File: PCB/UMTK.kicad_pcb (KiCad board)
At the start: 4 copper layers, 170 x 80 mm, 99 parts, among them J1 Motor Out, J2 ESTOP, J3 LOADCELL, J5 PJ-102BH, J8 10033526-N3212LF, Q1 Q_PNP_BEC, U1 DRV8873SPWPRQ1, U10 LM2576HVS-5, U11 SN74LVC1T45DCK, U12 SN74LVC1T45DCK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

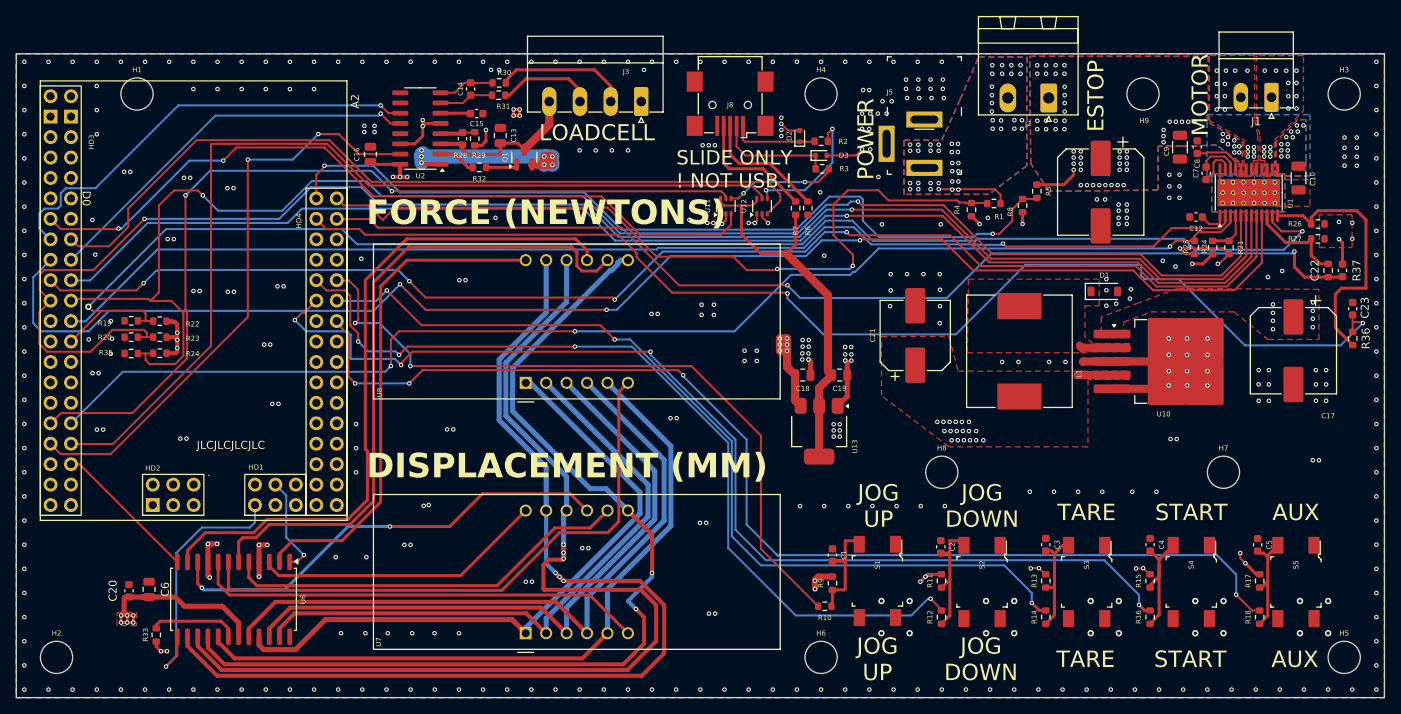
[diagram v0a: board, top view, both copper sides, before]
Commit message: Update PCB to seperate ground symbols apporiately. Modify board to sepearte ground path for motor current and all other devices. Add filtering for slide power, hopefully reduce bownout or other issue.
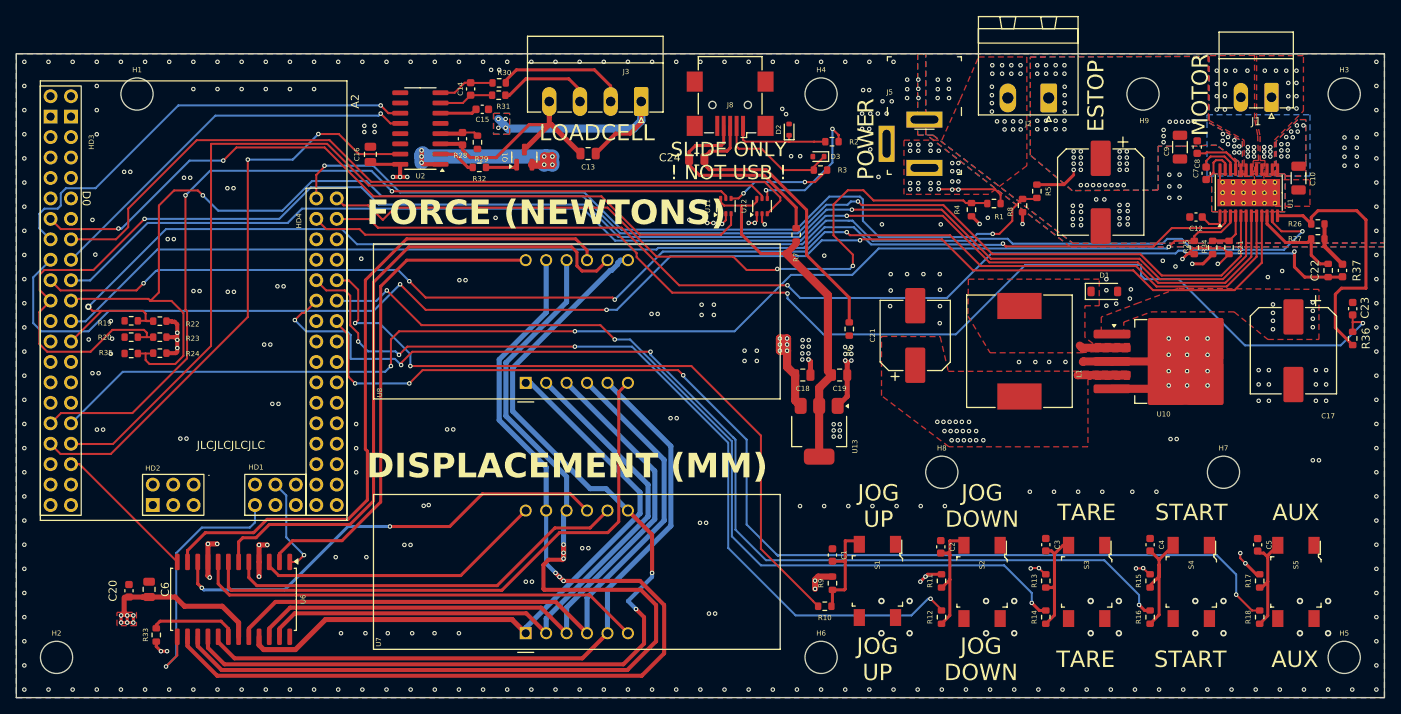
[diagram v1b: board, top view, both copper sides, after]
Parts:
- added C24: 10u, Capacitor_SMD:C_0805_2012Metric, F.Cu at (104.5, 33.1)
- moved R6 15.9 mm to (123.5, 54.2)
- moved C13 11.1 mm to (91.0, 32.4), turned to 180 degrees
- moved R7 3.32 mm to (116.9, 42.5)
- moved D2 1.55 mm to (116.0, 29.4)
- moved R2 1.34 mm to (121.3, 30.9)
- moved C15 0.88 mm to (77.9, 26.9)
- moved R29 0.56 mm to (77.3, 31.0)
- moved D3 0.37 mm to (119.7, 32.8), turned to 180 degrees
- moved R3 0.27 mm to (119.9, 34.5)
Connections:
- net GND renamed GNDA
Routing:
- net Net-(J8-D+): track 15.6 -> 38.6 mm
- net GNDA: track 72.7 -> 84.5 mm, vias 427 -> 416
- net Net-(J8-ID): track 15.6 -> 26.6 mm
- net /HX711/LCE+: track 20.0 -> 30.5 mm
- net +3V3: track 49.4 -> 46.1 mm
- net Net-(D2-K): track 10.6 -> 12.9 mm
- net Net-(D3-K): track 14.5 -> 15.6 mm
- net /Arduino/SLIDE_DAT: track 101.2 -> 100.2 mm
- net Net-(U2-VBG): track 3.67 -> 4.62 mm
- net Net-(U2-VFB): track 3.85 -> 4.61 mm
- net +12V: vias 56 -> 50
- added copper zone on In1.Cu, net GNDA
- removed copper zone on B.Cu, net +12V
- removed copper zone on In2.Cu, net +12V

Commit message: WIP Adding adudino onboard, so far copying pro mega
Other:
- board text added: "UMTK V1.6"
- board text removed: "UMTK V1.5"
